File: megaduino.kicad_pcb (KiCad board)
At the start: 2 copper layers, 48.9 x 52.7 mm, 38 parts, among them J1 Conn_01x20_Female, J2 Conn_01x20_Female, J3 Conn_01x13_Male, J4 Conn_01x02_Male, J5 Conn_01x04_Male, Q1 RFD14N05L, Q2 RFD14N05L, U1 LMV324, U2 MCP2562-E-SN, U3 LMV324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

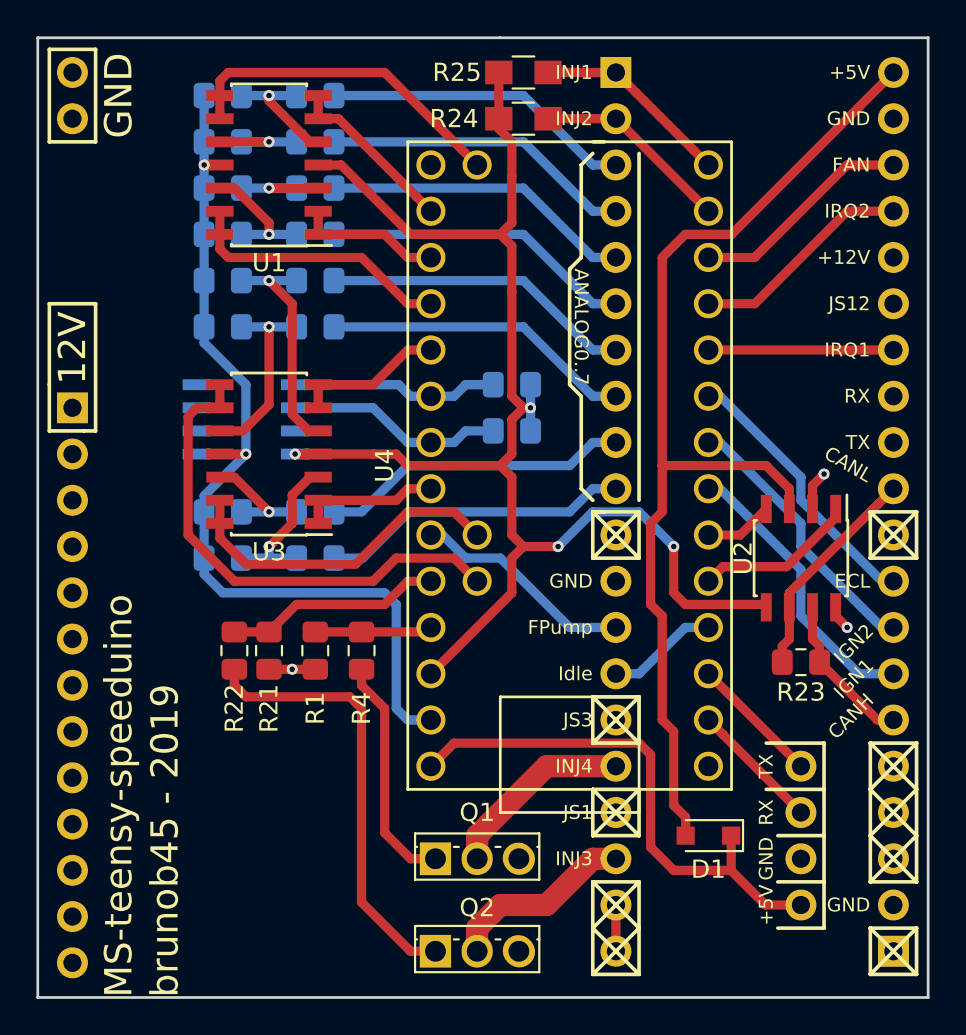
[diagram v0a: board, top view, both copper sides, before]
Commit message: pull-up on ignition and move IGN3-4 transistors away from usb connector
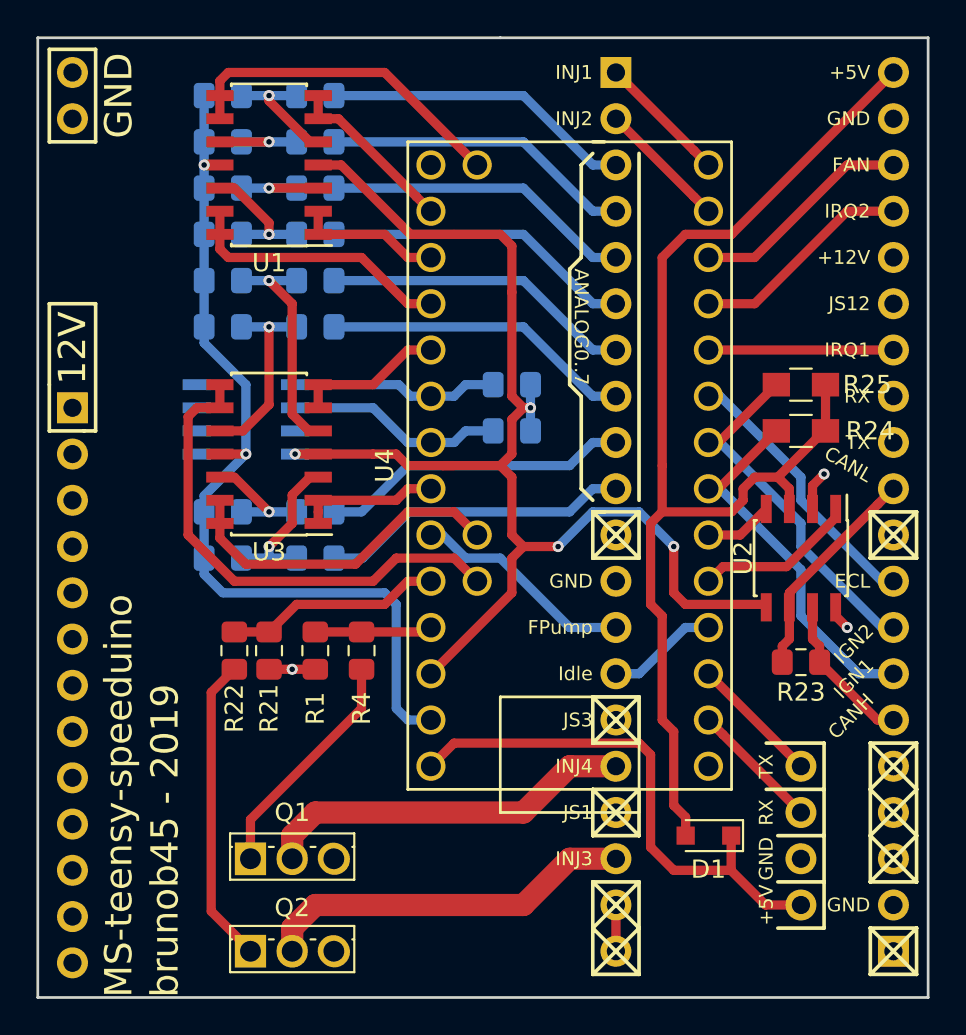
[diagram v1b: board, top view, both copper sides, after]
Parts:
- moved R24 22.9 mm to (160.0, 88.3), turned to 180 degrees
- moved R25 22.9 mm to (160.0, 85.7), turned to 180 degrees
- moved Q1 10.2 mm to (129.8, 111.8)
- moved Q2 10.2 mm to (129.8, 116.8)
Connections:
- R24 pad 1: +3V3 -> +5V
- R24 pad 2: INJ2 -> IGN1
- R25 pad 1: +3V3 -> +5V
- R25 pad 2: INJ1 -> IGN2
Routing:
- net JS2: track 10.5 -> 20.6 mm
- net JS0: track 10.5 -> 20.6 mm
- net +3V3: track 81.7 -> 72.3 mm
- net Net-(Q2-Pad1): track 25.3 -> 17.4 mm
- net +5V: track 58.3 -> 65.4 mm
- net IGN2: track 15.1 -> 20.2 mm
- net IGN1: track 15.9 -> 20.9 mm
- net INJ1: track 11.1 -> 7.18 mm
- net INJ2: track 10.9 -> 7.18 mm
